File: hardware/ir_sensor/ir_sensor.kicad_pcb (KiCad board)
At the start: 2 copper layers, 45.5 x 71 mm, 32 parts, among them J1 Conn_01x04, J10 Conn_01x02, J11 Conn_01x02, J12 Conn_01x02, J13 Conn_01x02, J2 Conn_01x04, J3 Conn_01x04, J4 Conn_01x02, J5 Conn_01x02, J6 Conn_01x02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

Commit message: boards review
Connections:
- J10 pad 1: d_4 -> +3V3
- J10 pad 2: GND -> d_4
- J11 pad 1: d_2 -> +3V3
- J11 pad 2: GND -> d_2
- J12 pad 1: d_5 -> +3V3
- J12 pad 2: GND -> d_5
- J13 pad 1: d_3 -> +3V3
- J13 pad 2: GND -> d_3
- J9 pad 1: d_1 -> +3V3
- J9 pad 2: GND -> d_1
- R10 pad 1: +3V3 -> d_3
- R10 pad 2: d_3 -> GND
- R11 pad 1: +3V3 -> d_2
- R11 pad 2: d_2 -> GND
- R12 pad 1: +3V3 -> d_5
- R12 pad 2: d_5 -> GND
- R13 pad 1: +3V3 -> d_4
- R13 pad 2: d_4 -> GND
- R2 pad 1: +3V3 -> d_1
- R2 pad 2: d_1 -> GND
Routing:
- net +3V3: track 39.4 -> 66.0 mm
- net d_2: track 46.3 -> 37.6 mm
- net d_3: track 40.5 -> 32.6 mm
- net d_1: track 28.1 -> 23.0 mm
- net d_4: track 48.4 -> 43.8 mm
- net d_5: track 38.3 -> 39.3 mm
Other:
- board text added: "IR board v0.3"
- board text removed: "IR board v0.2"

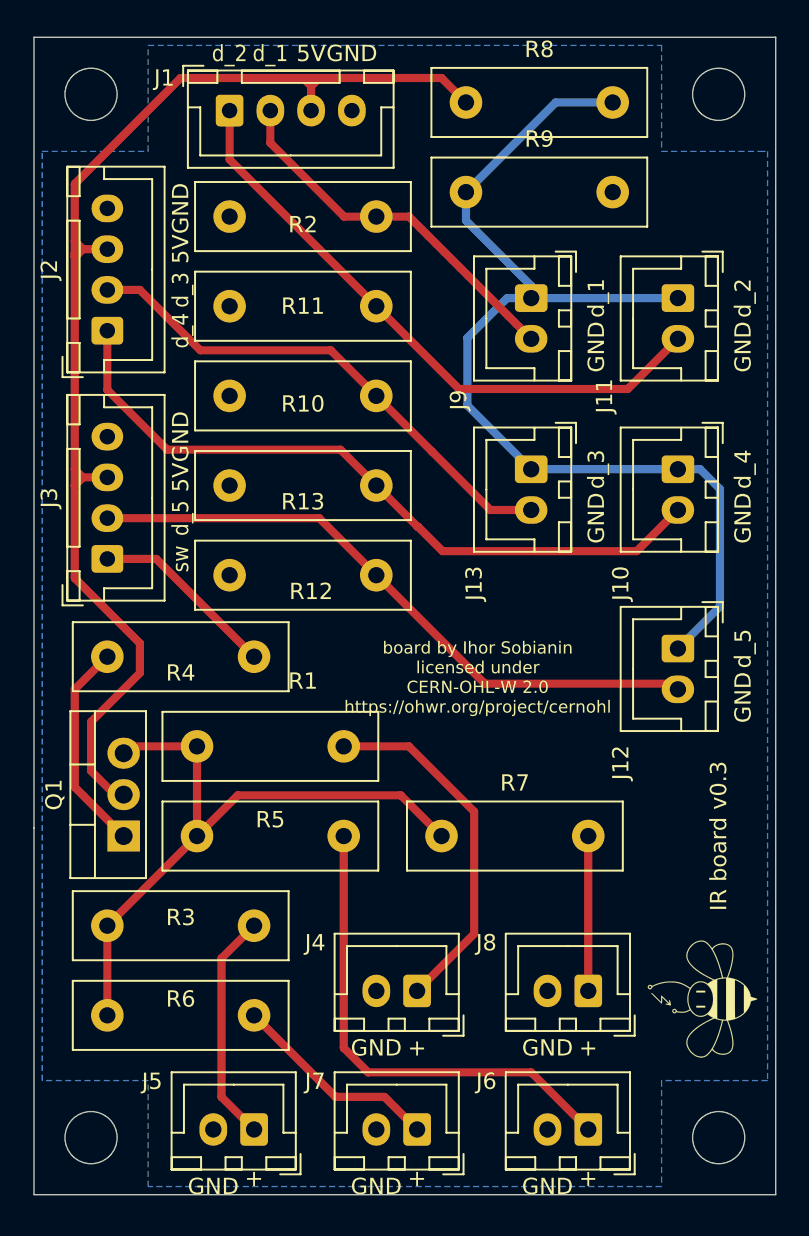
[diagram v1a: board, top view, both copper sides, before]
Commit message: Update IR sensor
MOSFET was wrongly connected to the LED thus rendering the PCB unusable. Now, it is connected the right way

Co-Authored-By: Andre Maia Chagas <a.maia-chagas@sussex.ac.uk>
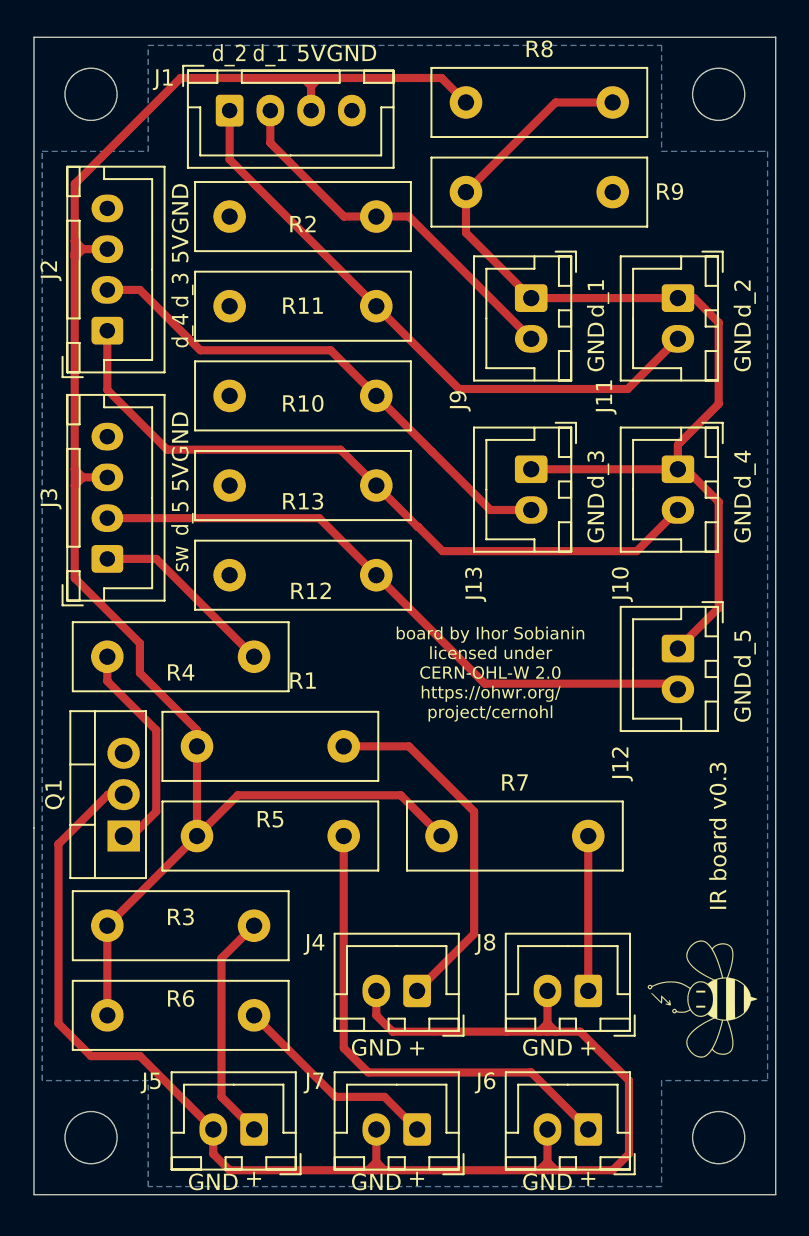
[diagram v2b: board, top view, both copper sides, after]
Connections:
- J4 pad 2: GND -> Vdrive
- J5 pad 2: GND -> Vdrive
- J6 pad 2: GND -> Vdrive
- J7 pad 2: GND -> Vdrive
- J8 pad 2: GND -> Vdrive
- Q1 pad 2: +5V -> Vdrive
- Q1 pad 3: Vdrive -> GND
- R1 pad 1: Vdrive -> +5V
- R3 pad 1: Vdrive -> +5V
- R5 pad 1: Vdrive -> +5V
- R6 pad 1: Vdrive -> +5V
- R7 pad 1: Vdrive -> +5V
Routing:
- net Vdrive: track 40.5 -> 91.7 mm
- net +5V: track 77.8 -> 109.8 mm
- net +3V3: track 66.0 -> 64.0 mm
- net d_3: track 32.6 -> 31.6 mm
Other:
- net class Default removed
- board text added: "board by Ihor Sobianin licensed under CERN-OHL-W 2.0 https://ohwr.org/ project/cernohl"
- board text removed: "board by Ihor Sobianin licensed under CERN-OHL-W 2.0 https://ohwr.org/project/cernohl"
